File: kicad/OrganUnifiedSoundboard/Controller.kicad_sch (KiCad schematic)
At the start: 16 parts, among them J11 GPIO, SW1 MODES, U1 ESP32-S3-DevKitC

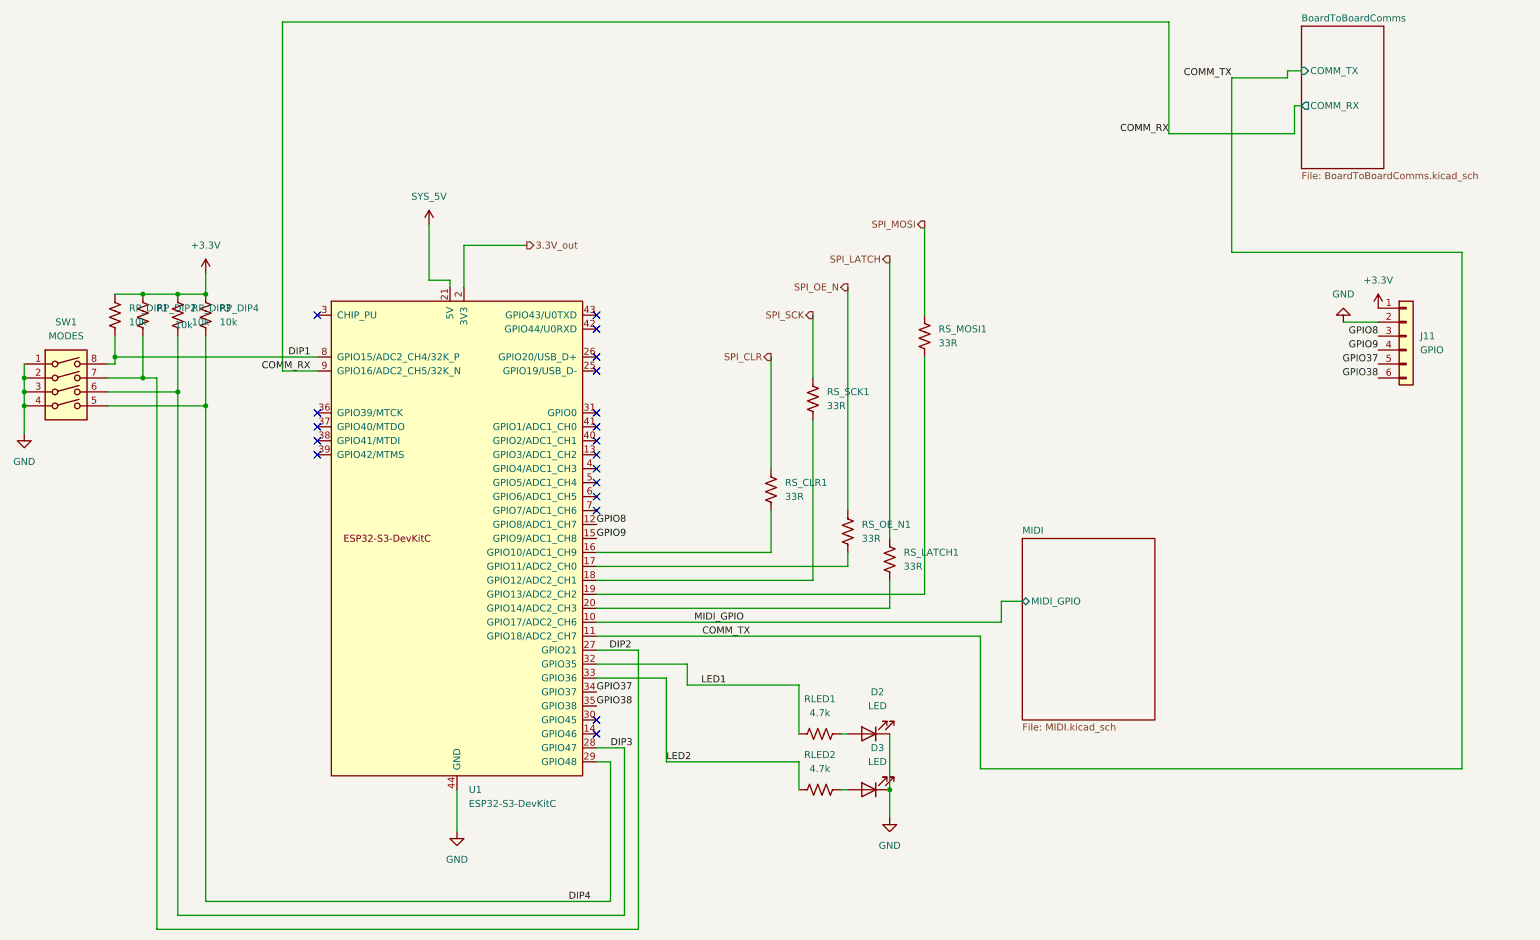
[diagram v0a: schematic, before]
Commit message: Adding some custom components that some of the kicad things depend on
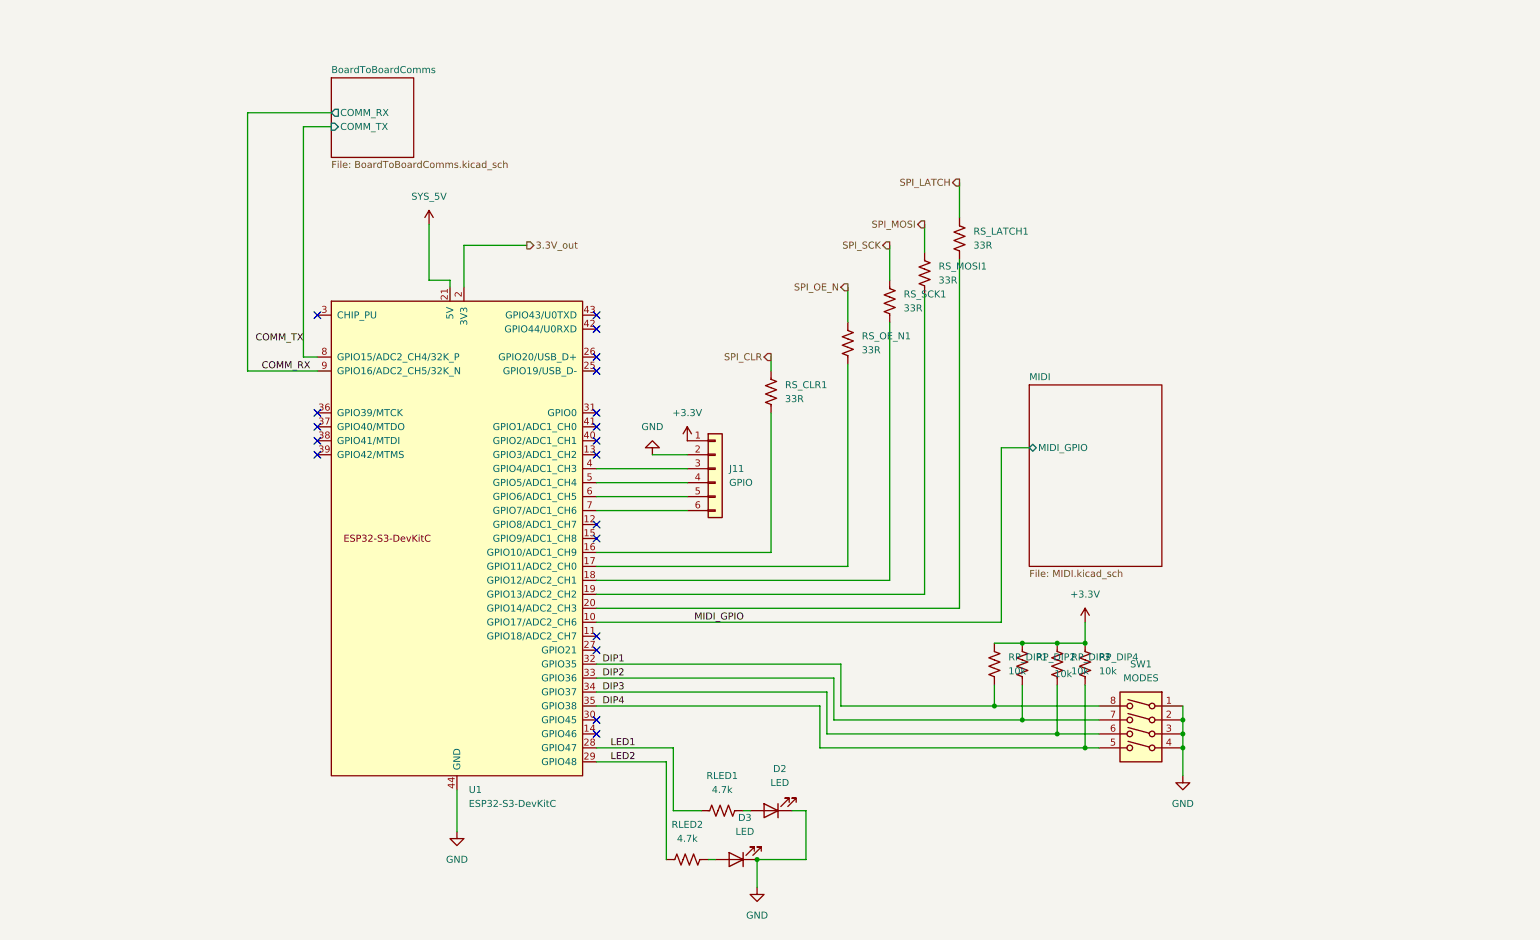
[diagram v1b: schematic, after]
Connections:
- net COMM_TX: now also U1.8 (GPIO15/ADC2_CH4/32K_P); no longer U1.11 (GPIO18/ADC2_CH7)
- net DIP1: now also U1.32 (GPIO35); no longer U1.8 (GPIO15/ADC2_CH4/32K_P)
- net DIP2: now also U1.33 (GPIO36); no longer U1.27 (GPIO21)
- net DIP3: now also U1.34 (GPIO37); no longer U1.28 (GPIO47)
- net DIP4: now also U1.35 (GPIO38); no longer U1.29 (GPIO48)
- net LED1: now also U1.28 (GPIO47); no longer U1.32 (GPIO35)
- net LED2: now also U1.29 (GPIO48); no longer U1.33 (GPIO36)
- net at U1.4 (GPIO4/ADC1_CH3): now also J11.3 (Pin_3)
- net at U1.5 (GPIO5/ADC1_CH4): now also J11.4 (Pin_4)
- net at U1.6 (GPIO6/ADC1_CH5): now also J11.5 (Pin_5)
- net at U1.7 (GPIO7/ADC1_CH6): now also J11.6 (Pin_6)
- removed net GPIO37: J11.5 (Pin_5), U1.34 (GPIO37)
- removed net GPIO38: J11.6 (Pin_6), U1.35 (GPIO38)
- net GPIO8: no longer names the net of U1.12 (GPIO8/ADC1_CH7)
- net GPIO8: no longer J11.3 (Pin_3)
- net GPIO9: no longer names the net of U1.15 (GPIO9/ADC1_CH8)
- net GPIO9: no longer J11.4 (Pin_4)
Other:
- moved on the sheet: D2, D3, J11, RLED1, RLED2, RP_DIP1, RP_DIP2, RP_DIP3, RP_DIP4, RS_CLR1, RS_LATCH1, RS_MOSI1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

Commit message: Finalized unified soundboard driver for production, adding some models
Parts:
- U1: footprint PCM_Espressif:ESP32-S3-DevKitC -> CustomLibrary:ESP32-S3-DevKitC-SHORTENED
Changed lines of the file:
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@@
+		(color 0 0 0 0)
+	)
+	(junction
+		(at 100.33 62.23)
+		(diameter 0)
 		(color 0 0 0 0)
 	)
@@
 	(wire
 		(pts
-			(xy 93.98 62.23) (xy 105.41 62.23)
+			(xy 93.98 62.23) (xy 100.33 62.23)
 		)
 		(stroke
@@
 		(pts
 			(xy 118.11 105.41) (xy 134.62 105.41)
+		)
+		(stroke
+			(width 0)
+			(type default)
+		)
+	)
+	(wire
+		(pts
+			(xy 100.33 62.23) (xy 105.41 62.23)
 		)
 		(stroke
@@
 			)
 		)
-		(property "Footprint" "PCM_Espressif:ESP32-S3-DevKitC"
+		(property "Footprint" "CustomLibrary:ESP32-S3-DevKitC-SHORTENED"
 			(at 92.71 172.72 0)
 			(effects
@@
 					(unit 1)
 				)
+			)
+		)
+	)
+	(symbol
+		(lib_id "power:PWR_FLAG")
+		(at 100.33 62.23 0)
+		(unit 1)
+		(exclude_from_sim no)
+		(in_bom yes)
+		(on_board yes)
+		(dnp no)
+		(fields_autoplaced yes)
+		(property "Reference" "#FLG03"
+			(at 100.33 60.325 0)
+			(effects
+				(font
+					(size 1.27 1.27)
+				)
+				(hide yes)
+			)
+		)
+		(property "Value" "PWR_FLAG"
+			(at 100.33 57.15 0)
+			(effects
+				(font
+					(size 1.27 1.27)
+				)
+			)
+		)
+		(property "Footprint" ""
+			(at 100.33 62.23 0)
+			(effects
+				(font
+					(size 1.27 1.27)
+				)
+				(hide yes)
+			)
+		)
+		(property "Datasheet" "~"
+			(at 100.33 62.23 0)
+			(effects
+				(font
+					(size 1.27 1.27)
+				)
+				(hide yes)
+			)
+		)
+		(property "Description" "Special symbol for telling ERC where power comes from"
+			(at 100.33 62.23 0)
+			(effects
+				(font
+					(size 1.27 1.27)
+				)
+				(hide yes)
+			)
+		)
+		(pin "1"
+		)
+		(instances
+			(project ""
+				(path "/4a899aa1-9bb8-4bd0-98b8-a923f79fe9df/cfa6cbaf-d0e0-41c4-8de8-02a89a1099b2"
+					(reference "#FLG03")
+					(unit 1)
+				)
